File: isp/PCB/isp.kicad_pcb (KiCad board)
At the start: 2 copper layers, 33 x 14 mm, 19 parts, among them J1 PC, J2 12V, J3 AVR-ISP-6, J4 POW_SEL, J5 USART, Q1 2N7002, Q2 2N7002, Q3 2N7002, U1 ATtiny25-20P

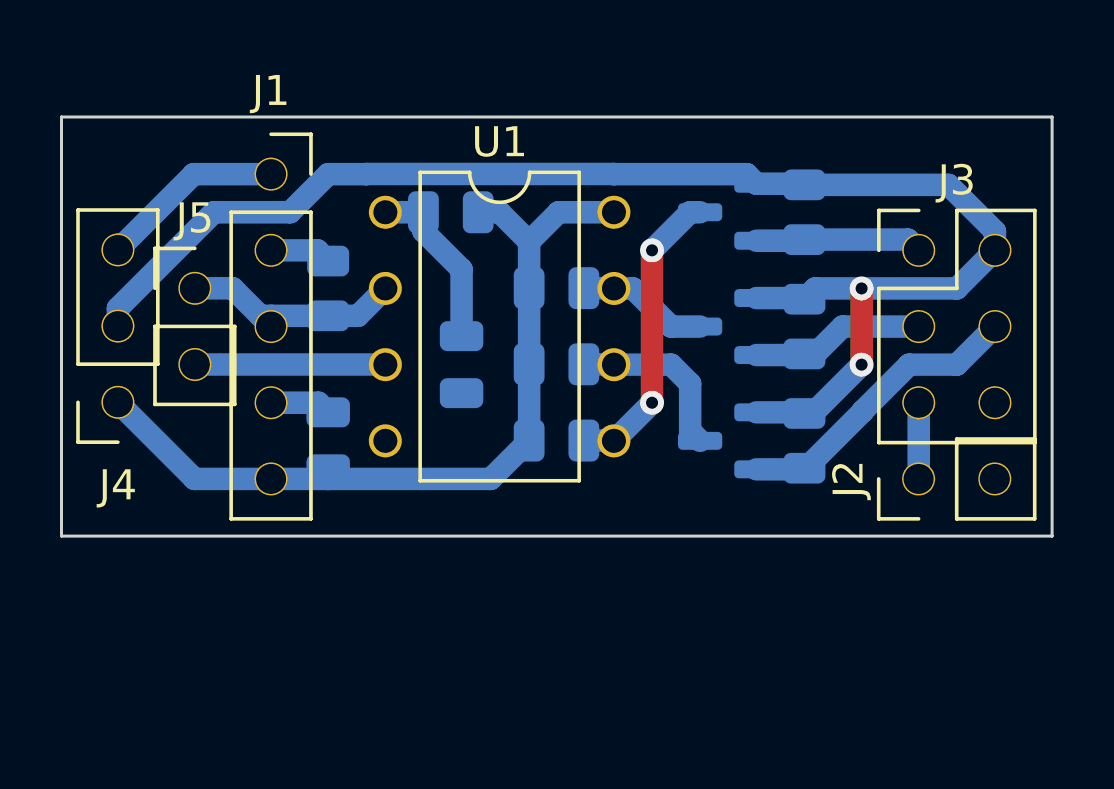
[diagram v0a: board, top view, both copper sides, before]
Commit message: Optimize ISP circuit - Add ISP reset button and target enable SW - Change ISP output level shifter from NMOS to diode (save space & cost) - Rearrang PCB to save size, some SMD on back can overlap with USB board - Add a LED
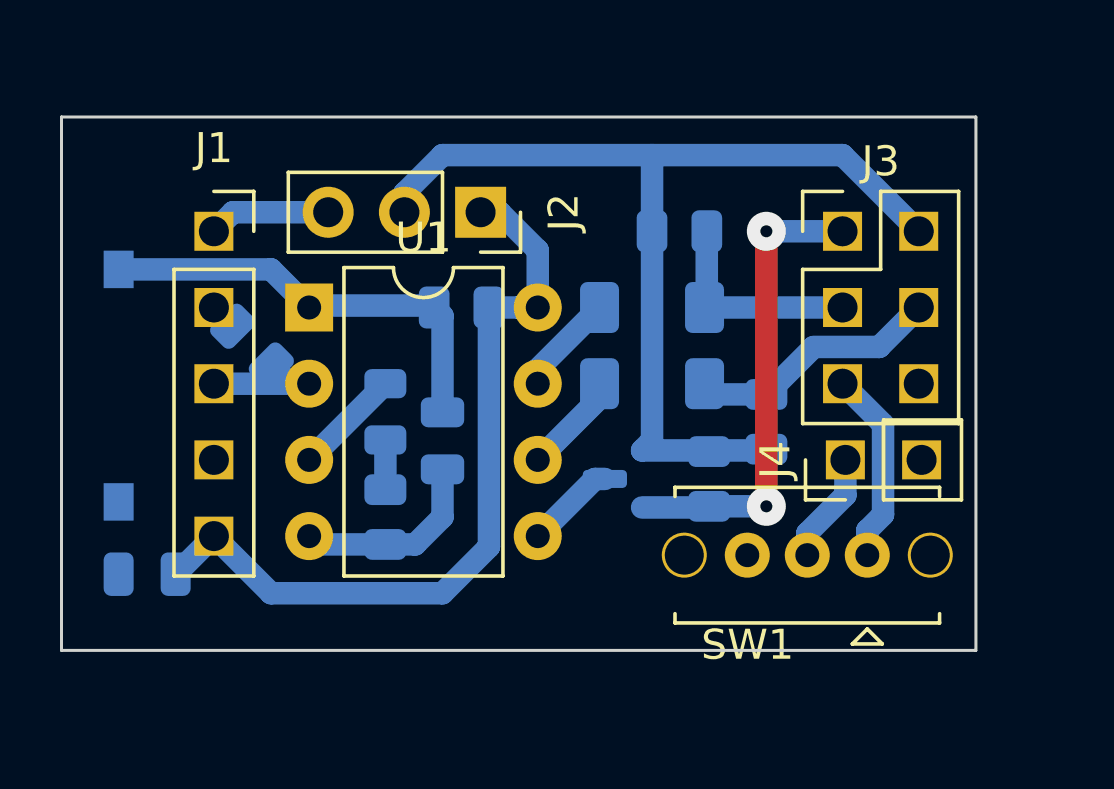
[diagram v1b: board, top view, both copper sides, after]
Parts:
- removed J5: USART, Connector_PinHeader_2.54mm:PinHeader_1x02_P2.54mm_Vertical
- removed Q2, Q3: 2N7002, Package_TO_SOT_SMD:SOT-23
- removed R7, R8: 500, Resistor_SMD:R_0805_2012Metric
- added D1: LL4148, Diode_SMD:D_MiniMELF, B.Cu at (19.7, 8.89)
- added D2: LL4148, Diode_SMD:D_MiniMELF, B.Cu at (19.7, 6.35)
- added D3: LED, LED_SMD:LED_0805_2012Metric, B.Cu at (10.8, 9.83)
- added SW1: ENABLE, Button_Switch_THT:SW_Slide_1P2T_CK_OS102011MS2Q, F.Cu at (26.9, 14.6)
- added SW2: RESET, Button_Switch_SMD:SW_Tactile_SPST_NO_Straight_CK_PTS636Sx25SMTRLFS, B.Cu at (1.91, 8.96)
- J2: value 12V -> POW_SEL; footprint Connector_PinHeader_2.54mm:PinHeader_1x02_P2.54mm_Vertical -> Connector_PinSocket_2.54mm:PinSocket_1x03_P2.54mm_Vertical
- J4: value POW_SEL -> 12V; footprint Connector_PinSocket_2.54mm:PinSocket_1x03_P2.54mm_Vertical -> Connector_PinHeader_2.54mm:PinHeader_1x02_P2.54mm_Vertical
- R2, R4: value 500 -> 20k
- R3: value 10k -> 20k
- R5, R6: value 500 -> 10k
- moved J4 24.3 mm to (26.1, 11.4), turned to 90 degrees
- moved J2 17.1 mm to (14.0, 3.17), turned to -90 degrees
- moved R3 12.6 mm to (23.5, 10.2), turned to 90 degrees
- moved C1 12.6 mm to (2.85, 15.2), turned to 180 degrees
- moved R6 11.4 mm to (13.3, 6.35), turned to 0 degrees
- moved R4 6.36 mm to (21.6, 12.1), turned to -90 degrees
- moved R5 6.25 mm to (10.8, 13.3), turned to -90 degrees
- moved Q1 5.99 mm to (19.1, 12.1)
- moved R2 4.51 mm to (20.6, 3.81)
- moved U1 4.07 mm to (8.26, 6.35)
- moved C2 3.81 mm to (12.7, 10.8), turned to -90 degrees
- moved R1 3.18 mm to (6.35, 7.62), turned to -45 degrees
- moved J1 2.69 mm to (5.08, 3.81)
- moved J3 2.62 mm to (26.0, 3.81)
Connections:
- C1 pad 1: Net-(U1-~{RESET}/PB5) -> +5V
- C2 pad 1: +5V -> Net-(U1-~{RESET}/PB5)
- J2 pad 1: Net-(J2-Pin_1) -> +5V
- J2 pad 2: GND -> Net-(J2-Pin_2)
- J3 pad 2: Net-(J3-VCC) -> Net-(J2-Pin_2)
- J3 pad 3: Net-(J3-SCK) -> Net-(D2-A)
- J3 pad 4: Net-(J3-MOSI) -> Net-(D1-A)
- J3 pad 5: Net-(J2-Pin_1) -> Net-(J3-~{RST})
- J4 pad 1: +5V -> Net-(J4-Pin_1)
- J4 pad 2: Net-(J3-VCC) -> GND
- Q1 pad 1: Net-(J3-VCC) -> Net-(J2-Pin_2)
- Q1 pad 2: Net-(J3-SCK) -> Net-(J3-MISO)
- R2 pad 1: +5V -> Net-(J2-Pin_2)
- R2 pad 2: Net-(Q1-D) -> Net-(D2-A)
- R3 pad 1: Net-(U1-~{RESET}/PB5) -> Net-(J2-Pin_2)
- R3 pad 2: +5V -> Net-(D1-A)
- R4 pad 1: +5V -> Net-(J2-Pin_2)
- R4 pad 2: Net-(Q2-D) -> Net-(J3-MISO)
- R5 pad 1: +5V -> Net-(D3-K)
- R5 pad 2: Net-(Q3-D) -> GND
- R6 pad 1: Net-(J3-VCC) -> Net-(U1-~{RESET}/PB5)
- R6 pad 2: Net-(J3-SCK) -> +5V
- U1 pad 3: UCLK -> Net-(D3-A)
- U1 pad 5: Net-(Q3-D) -> Net-(Q1-D)
- U1 pad 6: Net-(Q2-D) -> Net-(D1-K)
- U1 pad 7: Net-(Q1-D) -> Net-(D2-K)
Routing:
- net Net-(J3-VCC): track 48.5 -> 0.00 mm, vias 2 -> 0
- net Net-(J2-Pin_2): track 0.00 -> 33.5 mm
- net Net-(J3-MISO): track 5.58 -> 15.9 mm, vias 0 -> 2
- net Net-(Q3-D): track 10.0 -> 0.00 mm, vias 2 -> 0
- net Net-(J3-MOSI): track 9.93 -> 0.00 mm
- net Net-(U1-~{RESET}/PB5): track 5.93 -> 14.7 mm
- net Net-(D1-A): track 0.00 -> 8.48 mm
- net Net-(D2-A): track 0.00 -> 7.19 mm
- net Net-(J3-~{RST}): track 0.00 -> 6.49 mm
- net UCLK: track 6.35 -> 0.00 mm
- net Net-(Q2-D): track 5.85 -> 0.00 mm
- net Net-(J3-SCK): track 5.81 -> 0.00 mm
- net GND: track 2.04 -> 6.53 mm
- net Net-(J4-Pin_1): track 0.00 -> 3.70 mm
- net Net-(D3-A): track 0.00 -> 3.59 mm
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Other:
- board size 33 x 14 mm -> 30.5 x 17.8 mm

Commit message: ISP speed change: 9600 --> 115200 - Increase speed: Data stream (EEPROM/Flash) transfer at 9600BAUD is too slow (9600 only good for fuse). - Reduce resistor (50k --> 5k), Pull-up time too long for 50kR, OK for 1MHz but gives error when talk to 8MHz AVR. - Note: target AVR response to clk too fast. Signal propagation is not fast enough due to long rise time.
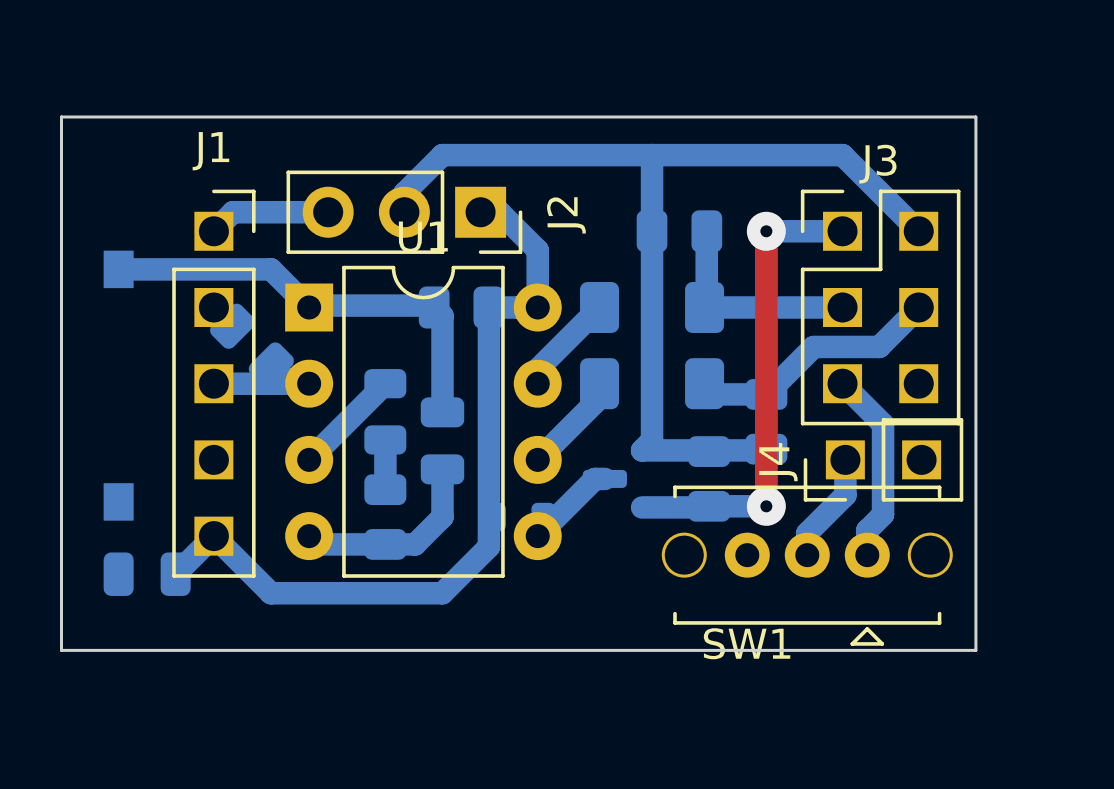
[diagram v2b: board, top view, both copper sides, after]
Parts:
- added R7: 5k, Resistor_SMD:R_0603_1608Metric, B.Cu at (15.2, 13.3)
- R2, R3, R4: value 20k -> 5k
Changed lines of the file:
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@@
       (net 16 "Net-(J4-Pin_1)") (pinfunction "B") (pintype "passive"))
     (pad "3" thru_hole circle (at 4 0 180) (size 1.5 1.5) (drill 0.8) (layers "*.Cu" "*.Mask")
-      (net 18 "unconnected-(SW1-C-Pad3)") (pinfunction "C") (pintype "passive"))
+      (net 18 "unconnected-(SW1-C-Pad3)") (pinfunction "C") (pintype "passive+no_connect"))
     (model "${KICAD6_3DMODEL_DIR}/Button_Switch_THT.3dshapes/SW_Slide_1P2T_CK_OS102011MS2Q.wrl"
       (offset (xyz 0 0 0))
@@
     )
   )
+  (footprint "Resistor_SMD:R_0603_1608Metric" (layer "B.Cu")
+    (at 15.24 13.335)
+    (descr "Resistor SMD 0603 (1608 Metric), square (rectangular) end terminal, IPC_7351 nominal, (Body size source: IPC-SM-782 page 72, https://www.pcb-3d.com/wordpress/wp-content/uploads/ipc-sm-782a_amendment_1_and_2.pdf), generated with kicad-footprint-generator")
+    (tags "resistor")
+    (property "Sheetfile" "isp.kicad_sch")
+    (property "Sheetname" "")
+    (property "ki_description" "Resistor, small US symbol")
+    (property "ki_keywords" "r resistor")
+    (attr smd)
+    (fp_text reference "R7" (at 0 1.43) (layer "B.SilkS")
+        (effects (font (size 1 1) (thickness 0.15)) (justify mirror))
+    )
+    (fp_text value "5k" (at 0 -1.43) (layer "B.Fab")
+        (effects (font (size 1 1) (thickness 0.15)) (justify mirror))
+    )
+    (fp_text user "${REFERENCE}" (at 0 0) (layer "B.Fab")
+        (effects (font (size 0.4 0.4) (thickness 0.06)) (justify mirror))
+    )
+    (fp_line (start -0.237258 -0.5225) (end 0.237258 -0.5225)
+      (stroke (width 0.12) (type solid)) (layer "B.SilkS"))
+    (fp_line (start -0.237258 0.5225) (end 0.237258 0.5225)
+      (stroke (width 0.12) (type solid)) (layer "B.SilkS"))
+    (fp_line (start -1.48 -0.73) (end -1.48 0.73)
+      (stroke (width 0.05) (type solid)) (layer "B.CrtYd"))
+    (fp_line (start -1.48 0.73) (end 1.48 0.73)
+      (stroke (width 0.05) (type solid)) (layer "B.CrtYd"))
+    (fp_line (start 1.48 -0.73) (end -1.48 -0.73)
+      (stroke (width 0.05) (type solid)) (layer "B.CrtYd"))
+    (fp_line (start 1.48 0.73) (end 1.48 -0.73)
+      (stroke (width 0.05) (type solid)) (layer "B.CrtYd"))
+    (fp_line (start -0.8 -0.4125) (end -0.8 0.4125)
+      (stroke (width 0.1) (type solid)) (layer "B.Fab"))
+    (fp_line (start -0.8 0.4125) (end 0.8 0.4125)
+      (stroke (width 0.1) (type solid)) (layer "B.Fab"))
+    (fp_line (start 0.8 -0.4125) (end -0.8 -0.4125)
+      (stroke (width 0.1) (type solid)) (layer "B.Fab"))
+    (fp_line (start 0.8 0.4125) (end 0.8 -0.4125)
+      (stroke (width 0.1) (type solid)) (layer "B.Fab"))
+    (pad "1" smd roundrect (at -0.825 0) (size 0.8 0.95) (layers "B.Cu" "B.Paste" "B.Mask") (roundrect_rratio 0.25)
+      (net 5 "+5V") (pintype "passive"))
+    (pad "2" smd roundrect (at 0.825 0) (size 0.8 0.95) (layers "B.Cu" "B.Paste" "B.Mask") (roundrect_rratio 0.25)
+      (net 17 "Net-(Q1-D)") (pintype "passive"))
+    (model "${KICAD6_3DMODEL_DIR}/Resistor_SMD.3dshapes/R_0603_1608Metric.wrl"
+      (offset (xyz 0 0 0))
+      (scale (xyz 1 1 1))
+      (rotate (xyz 0 0 0))
+    )
+  )
   (footprint "Resistor_SMD:R_0805_2012Metric" (layer "B.Cu")
     (at 10.795 13.335 -90)
@@
         (effects (font (size 1 1) (thickness 0.15)) (justify mirror))
     )
-    (fp_text value "20k" (at 0 -1.65 90) (layer "B.Fab")
+    (fp_text value "5k" (at 0 -1.65 90) (layer "B.Fab")
         (effects (font (size 1 1) (thickness 0.15)) (justify mirror))
     )
@@
         (effects (font (size 1 1) (thickness 0.15)) (justify mirror))
     )
-    (fp_text value "20k" (at 0 -1.65 90) (layer "B.Fab")
+    (fp_text value "5k" (at 0 -1.65 90) (layer "B.Fab")
         (effects (font (size 1 1) (thickness 0.15)) (justify mirror))
     )
@@
         (effects (font (size 1 1) (thickness 0.15)) (justify mirror))
     )
-    (fp_text value "20k" (at 0 -1.65) (layer "B.Fab")
+    (fp_text value "5k" (at 0 -1.65) (layer "B.Fab")
         (effects (font (size 1 1) (thickness 0.15)) (justify mirror))
     )
@@
     (connect_pads (clearance 0.508))
     (min_thickness 0.25) (filled_areas_thickness no)
-    (fill yes (thermal_gap 0.5) (thermal_bridge_width 0.5) (island_removal_mode 1) (island_area_min 10))
+    (fill yes (thermal_gap 0.3) (thermal_bridge_width 0.8) (island_removal_mode 1) (island_area_min 10))
     (polygon
       (pts

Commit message: New PCB design: Switch from tiny25 to tiny441/841
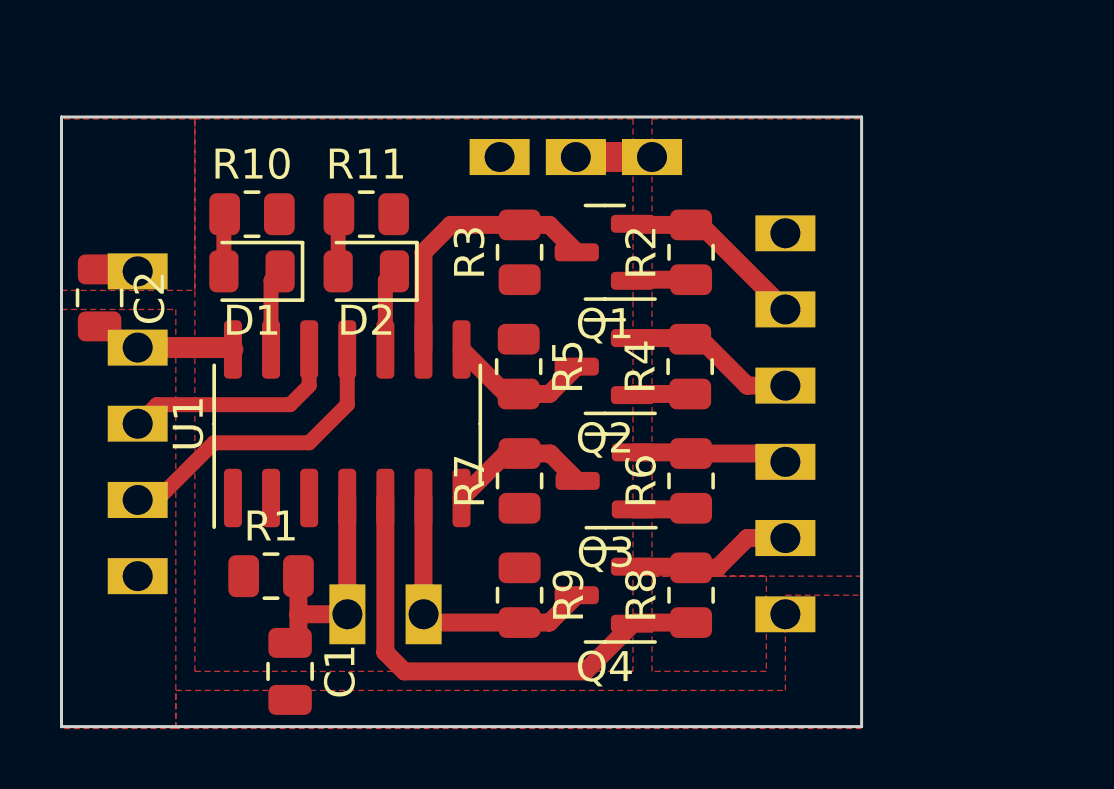
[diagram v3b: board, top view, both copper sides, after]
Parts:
- removed D3: LED, LED_SMD:LED_0805_2012Metric
- removed SW1: ENABLE, Button_Switch_THT:SW_Slide_1P2T_CK_OS102011MS2Q
- removed SW2: RESET, Button_Switch_SMD:SW_Tactile_SPST_NO_Straight_CK_PTS636Sx25SMTRLFS
- added Q2: 2N7002, Package_TO_SOT_SMD:SOT-23, F.Cu at (18.1, 8.32)
- added Q3: 2N7002, Package_TO_SOT_SMD:SOT-23, F.Cu at (18.1, 12.1)
- added Q4: 2N7002, Package_TO_SOT_SMD:SOT-23, F.Cu at (18.1, 15.9)
- added R10: 10k, Resistor_SMD:R_0805_2012Metric, F.Cu at (6.35, 3.24)
- added R11: 10k, Resistor_SMD:R_0805_2012Metric, F.Cu at (10.2, 3.24)
- added R8: 10k, Resistor_SMD:R_0805_2012Metric, F.Cu at (21.0, 15.9)
- added R9: 10k, Resistor_SMD:R_0805_2012Metric, F.Cu at (15.3, 15.9)
- C1, C2, Q1, R5, R6: moved to F.Cu
- D1, D2: value LL4148 -> LED; footprint Diode_SMD:D_MiniMELF -> LED_SMD:LED_0805_2012Metric; moved to F.Cu
- J1: footprint Connector_PinSocket_2.54mm:PinSocket_1x05_P2.54mm_Vertical -> Connector_PinHeader_2.54mm:PinHeader_1x05_P2.54mm_Vertical; moved to B.Cu
- J2: footprint Connector_PinSocket_2.54mm:PinSocket_1x03_P2.54mm_Vertical -> Connector_PinHeader_2.54mm:PinHeader_1x03_P2.54mm_Vertical; moved to B.Cu
- J3: value AVR-ISP-6 -> ISPRST; footprint Connector_PinHeader_2.54mm:PinHeader_2x03_P2.54mm_Vertical -> Connector_PinHeader_2.54mm:PinHeader_1x02_P2.54mm_Vertical; moved to B.Cu
- J4: value 12V -> ISP; footprint Connector_PinHeader_2.54mm:PinHeader_1x02_P2.54mm_Vertical -> Connector_PinHeader_2.54mm:PinHeader_1x06_P2.54mm_Vertical; moved to B.Cu
- R1: value 4.7k -> 10k; moved to F.Cu
- R2, R3, R4: value 5k -> 10k; moved to F.Cu
- R7: value 5k -> 10k; footprint Resistor_SMD:R_0603_1608Metric -> Resistor_SMD:R_0805_2012Metric; moved to F.Cu
- U1: value ATtiny25-20P -> ATtiny841-SS; footprint Package_DIP:DIP-8_W7.62mm -> Package_SO:SOIC-14_3.9x8.7mm_P1.27mm
- moved J3 18.9 mm to (12.1, 16.6), turned to 90 degrees
- moved D1 13.9 mm to (6.35, 5.14), turned to 180 degrees
- moved C2 12.4 mm to (1.27, 6.03)
- moved J1 11.8 mm to (2.54, 15.3)
- moved R3 9.98 mm to (15.3, 4.51)
- moved D2 9.60 mm to (10.2, 5.14), turned to 180 degrees
- moved R6 9.59 mm to (21.0, 12.1), turned to 90 degrees
- moved J4 7.82 mm to (24.1, 3.88), turned to 180 degrees
- moved R1 7.71 mm to (6.99, 15.3), turned to 0 degrees
- moved Q1 7.61 mm to (18.1, 4.51)
- moved R5 6.70 mm to (15.2, 8.32)
- moved C1 5.76 mm to (7.62, 18.5), turned to -90 degrees
- moved U1 4.08 mm to (9.53, 10.2), turned to 90 degrees
- moved R4 3.80 mm to (21.0, 8.32), turned to 90 degrees
- moved J2 1.95 mm to (14.6, 1.33)
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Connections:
- C1 pad 1: +5V -> Net-(J3-Pin_2)
- C2 pad 1: Net-(U1-~{RESET}/PB5) -> +5V
- J1 pad 1: +3V3 -> +3.3V
- J1 pad 2: Net-(J1-Pin_2) -> Rx
- J1 pad 3: UART -> Tx
- J2 pad 2: Net-(J2-Pin_2) -> VCC
- J2 pad 3: +3V3 -> VCC
- J3 pad 1: Net-(J3-MISO) -> RST
- J3 pad 2: Net-(J2-Pin_2) -> Net-(J3-Pin_2)
- J4 pad 1: Net-(J4-Pin_1) -> VCC
- J4 pad 2: GND -> Net-(J4-Pin_2)
- Q1 pad 1: Net-(J2-Pin_2) -> VCC
- Q1 pad 2: Net-(J3-MISO) -> Net-(J4-Pin_2)
- Q1 pad 3: Net-(Q1-D) -> SCK/Rx
- R1 pad 1: Net-(J1-Pin_2) -> +5V
- R1 pad 2: UART -> Net-(J3-Pin_2)
- R2 pad 1: Net-(J2-Pin_2) -> VCC
- R2 pad 2: Net-(D2-A) -> Net-(J4-Pin_2)
- R3 pad 1: Net-(J2-Pin_2) -> +5V
- R3 pad 2: Net-(D1-A) -> SCK/Rx
- R4 pad 1: Net-(J2-Pin_2) -> VCC
- R4 pad 2: Net-(J3-MISO) -> Net-(J4-Pin_3)
- R5 pad 1: Net-(D3-K) -> +5V
- R5 pad 2: GND -> MISO/Tx
- R6 pad 1: Net-(U1-~{RESET}/PB5) -> VCC
- R6 pad 2: +5V -> Net-(J4-Pin_4)
- R7 pad 2: Net-(Q1-D) -> MOSI/Xck
- U1 pad 1: Net-(U1-~{RESET}/PB5) -> +5V
- U1 pad 2: UART -> unconnected-(U1-XTAL1/PB0-Pad2)
- U1 pad 3: Net-(D3-A) -> unconnected-(U1-XTAL2/PB1-Pad3)
- U1 pad 4: GND -> Net-(J3-Pin_2)
- U1 pad 5: Net-(Q1-D) -> VCC
- U1 pad 6: Net-(D1-K) -> RST
- U1 pad 7: Net-(D2-K) -> MOSI/Xck
- U1 pad 8: +5V -> MISO/Tx
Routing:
- net Net-(J2-Pin_2): track 33.5 -> 0.00 mm
- net +5V: track 26.3 -> 0.00 mm
- net VCC: track 0.00 -> 24.6 mm
- net Net-(J3-MISO): track 15.9 -> 0.00 mm, vias 2 -> 0
- net Net-(U1-~{RESET}/PB5): track 14.7 -> 0.00 mm
- net Rx: track 0.00 -> 10.1 mm
- net RST: track 0.00 -> 9.47 mm
- net SCK/Rx: track 0.00 -> 9.11 mm
- net Tx: track 0.00 -> 7.45 mm
- net Net-(J3-Pin_2): track 0.00 -> 7.43 mm
- net Net-(D1-A): track 8.48 -> 1.92 mm
- net Net-(J3-~{RST}): track 6.49 -> 0.00 mm
- net Net-(J4-Pin_2): track 0.00 -> 6.26 mm
- net Net-(J4-Pin_3): track 0.00 -> 5.74 mm
- net Net-(J4-Pin_5): track 0.00 -> 5.51 mm
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- added copper zone on F.Cu, net +5V
- added copper zone on F.Cu, net GND
- added copper zone on F.Cu, net VCC
- removed copper zone on B.Cu, net GND
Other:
- board size 30.5 x 17.8 mm -> 26.7 x 20.3 mm
